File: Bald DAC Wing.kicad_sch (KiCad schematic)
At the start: 54 parts, among them J1 XTRA, J2 DAC_A_Out, J3 DAC_B_Out, J4 Data Debug HDR, J5 Z_Out, SW1 RESET, SW2 XTRA, U1 AD5447, U2 AD8065ARTZ, U3 AD8065ARTZ, U4 74LVC574APWR, U5 74LVC574APWR, U6 74LVC1G04, U7 REF3425

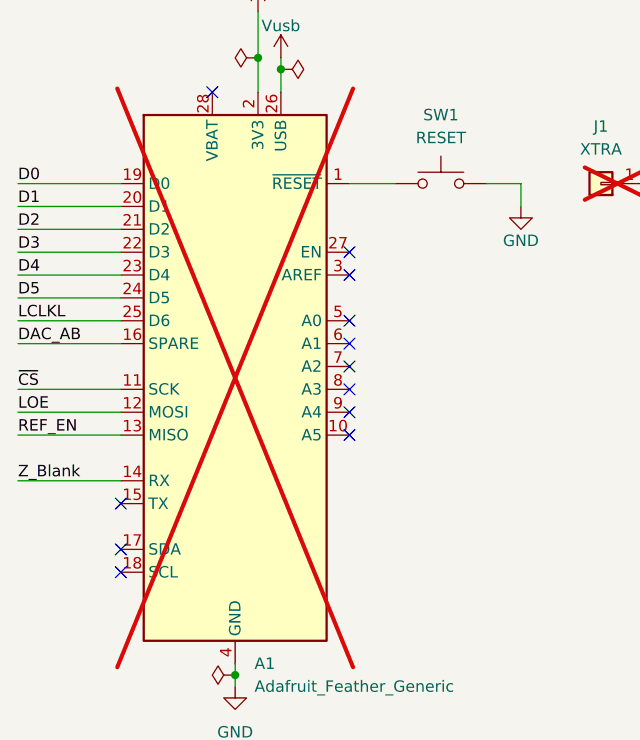
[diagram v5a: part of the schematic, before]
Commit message: only use 1/2 the feather!
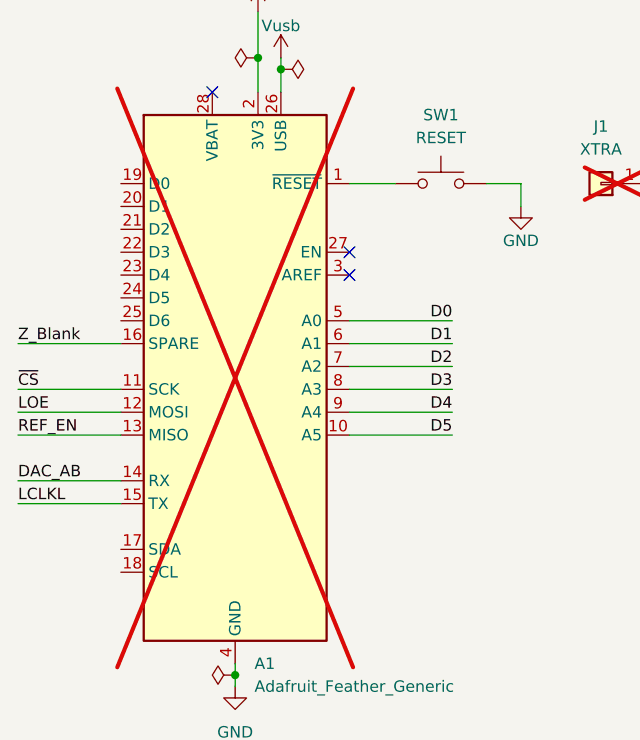
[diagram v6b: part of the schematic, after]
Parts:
- J4: footprint (none) -> Connector_PinHeader_2.00mm:PinHeader_2x16_P2.00mm_Vertical
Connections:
- net D0: now also A1.5 (A0); no longer A1.19 (D0)
- net D1: now also A1.6 (A1); no longer A1.20 (D1)
- net D2: now also A1.7 (A2); no longer A1.21 (D2)
- net D3: now also A1.8 (A3); no longer A1.22 (D3)
- net D4: now also A1.9 (A4); no longer A1.23 (D4)
- net D5: now also A1.10 (A5); no longer A1.24 (D5)
- net DAC_AB: now also A1.14 (RX); no longer A1.16 (SPARE)
- net LCLKL: now also A1.15 (TX); no longer A1.25 (D6)
- net Z_Blank: now also A1.16 (SPARE); no longer A1.14 (RX)
- no-connect marks 12 -> 3
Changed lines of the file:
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@@
 	)
 	(no_connect
-		(at 73.66 182.88)
-	)
-	(no_connect
-		(at 99.06 157.48)
-	)
-	(no_connect
-		(at 73.66 180.34)
-	)
-	(no_connect
-		(at 99.06 154.94)
-	)
-	(no_connect
-		(at 99.06 165.1)
-	)
-	(no_connect
 		(at 83.82 129.54)
 	)
@@
 	)
 	(no_connect
-		(at 73.66 175.26)
-	)
-	(no_connect
-		(at 99.06 167.64)
-	)
-	(no_connect
-		(at 99.06 160.02)
-	)
-	(no_connect
-		(at 99.06 162.56)
-	)
-	(no_connect
 		(at 99.06 147.32)
 	)
@@
 	(wire
 		(pts
-			(xy 62.23 139.7) (xy 73.66 139.7)
+			(xy 110.49 154.94) (xy 99.06 154.94)
 		)
 		(stroke
@@
 	(wire
 		(pts
-			(xy 62.23 154.94) (xy 73.66 154.94)
+			(xy 62.23 175.26) (xy 73.66 175.26)
 		)
 		(stroke
@@
 	(wire
 		(pts
-			(xy 62.23 147.32) (xy 73.66 147.32)
+			(xy 110.49 162.56) (xy 99.06 162.56)
 		)
 		(stroke
@@
 	(wire
 		(pts
-			(xy 62.23 172.72) (xy 73.66 172.72)
+			(xy 62.23 157.48) (xy 73.66 157.48)
 		)
 		(stroke
@@
 	(wire
 		(pts
-			(xy 62.23 144.78) (xy 73.66 144.78)
+			(xy 110.49 160.02) (xy 99.06 160.02)
 		)
 		(stroke
@@
 	(wire
 		(pts
-			(xy 269.24 87.63) (xy 279.4 87.63)
+			(xy 99.06 167.64) (xy 110.49 167.64)
 		)
 		(stroke
@@
 	(wire
 		(pts
-			(xy 62.23 152.4) (xy 73.66 152.4)
+			(xy 269.24 87.63) (xy 279.4 87.63)
 		)
 		(stroke
@@
 	(wire
 		(pts
-			(xy 62.23 142.24) (xy 73.66 142.24)
+			(xy 110.49 157.48) (xy 99.06 157.48)
 		)
 		(stroke
@@
 	(wire
 		(pts
-			(xy 62.23 149.86) (xy 73.66 149.86)
+			(xy 110.49 165.1) (xy 99.06 165.1)
 		)
 		(stroke
@@
 	(wire
 		(pts
-			(xy 62.23 157.48) (xy 73.66 157.48)
+			(xy 62.23 172.72) (xy 73.66 172.72)
 		)
 		(stroke
@@
 	)
 	(label "D3"
-		(at 62.23 147.32 0)
+		(at 110.49 162.56 180)
 		(effects
 			(font
 				(size 1.27 1.27)
 			)
-			(justify left bottom)
+			(justify right bottom)
 		)
 	)
@@
 	)
 	(label "D5"
-		(at 62.23 152.4 0)
+		(at 110.49 167.64 180)
 		(effects
 			(font
 				(size 1.27 1.27)
 			)
-			(justify left bottom)
+			(justify right bottom)
 		)
 	)
@@
 	)
 	(label "D0"
-		(at 62.23 139.7 0)
+		(at 110.49 154.94 180)
 		(effects
 			(font
 				(size 1.27 1.27)
 			)
-			(justify left bottom)
+			(justify right bottom)
 		)
 	)
@@
 	)
 	(label "D4"
-		(at 62.23 149.86 0)
+		(at 110.49 165.1 180)
 		(effects
 			(font
 				(size 1.27 1.27)
 			)
-			(justify left bottom)
+			(justify right bottom)
 		)
 	)
@@
 	)
 	(label "D1"
-		(at 62.23 142.24 0)
+		(at 110.49 157.48 180)
 		(effects
 			(font
 				(size 1.27 1.27)
 			)
-			(justify left bottom)
+			(justify right bottom)
 		)
 	)
@@
 	)
 	(label "Z_Blank"
-		(at 62.23 172.72 0)
+		(at 62.23 157.48 0)
 		(effects
 			(font
@@
 	)
 	(label "D2"
-		(at 62.23 144.78 0)
+		(at 110.49 160.02 180)
 		(effects
 			(font
 				(size 1.27 1.27)
 			)
-			(justify left bottom)
+			(justify right bottom)
 		)
 	)
@@
 	)
 	(label "LCLKL"
-		(at 62.23 154.94 0)
+		(at 62.23 175.26 0)
 		(effects
 			(font
@@
 	)
 	(label "DAC_AB"
-		(at 62.23 157.48 0)
+		(at 62.23 172.72 0)
 		(effects
 			(font
@@
 			)
 		)
-		(property "Footprint" ""
+		(property "Footprint" "Connector_PinHeader_2.00mm:PinHeader_2x16_P2.00mm_Vertical"
 			(at 245.11 124.46 0)
 			(hide yes)

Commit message: got rid of the switches
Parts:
- removed J1: XTRA, Connector_PinSocket_2.54mm:PinSocket_1x01_P2.54mm_Vertical, symbol Connector_Generic:Conn_01x01
- removed SW1: RESET, symbol Switch:SW_Push
- removed SW2: XTRA, symbol Switch:SW_Push
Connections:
- net D0: now also U4.9 (D7), U5.7 (D5); no longer U4.2 (D0), U5.2 (D0)
- net D1: now also U4.8 (D6), U5.6 (D4); no longer U4.3 (D1), U5.3 (D1)
- net D2: now also U4.7 (D5), U5.5 (D3); no longer U4.4 (D2), U5.4 (D2)
- net D3: now also U4.6 (D4), U5.4 (D2); no longer U4.5 (D3), U5.5 (D3)
- net D4: now also U4.5 (D3), U5.3 (D1); no longer U4.6 (D4), U5.6 (D4)
- net D5: now also U4.4 (D2), U5.2 (D0); no longer U4.7 (D5), U5.7 (D5)
- net DB10: now also U4.16 (Q3); no longer U4.18 (Q1)
- net DB11: now also U4.17 (Q2); no longer U4.19 (Q0)
- net DB6: now also U4.12 (Q7); no longer U4.14 (Q5)
- net DB7: now also U4.13 (Q6); no longer U4.15 (Q4)
- net DB8: now also U4.14 (Q5); no longer U4.16 (Q3)
- net DB9: now also U4.15 (Q4); no longer U4.17 (Q2)
- net at TP2.1: now also U4.18 (Q1); no longer U4.12 (Q7)
- net at TP1.1: now also U4.19 (Q0); no longer U4.13 (Q6)
- net at R70.2: now also U4.2 (D0); no longer U4.8 (D6)
- net at R69.2: now also U4.3 (D1); no longer U4.9 (D7)
- no-connect marks 3 -> 4
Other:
- moved on the sheet: R69, R70, TP1, TP2

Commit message: added power header
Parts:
- removed D2: PwrB+, LED_SMD:LED_0805_2012Metric_Pad1.15x1.40mm_HandSolder, symbol Device:LED
- removed D3: Vusb, LED_SMD:LED_0805_2012Metric_Pad1.15x1.40mm_HandSolder, symbol Device:LED
- removed R62, R63: 1k, Resistor_SMD:R_0603_1608Metric_Pad0.98x0.95mm_HandSolder, symbol Device:R
- added J1: PWR, Connector_PinHeader_2.54mm:PinHeader_1x02_P2.54mm_Vertical, symbol Connector_Generic:Conn_01x02
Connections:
- net +3V3: now also J1.2 (Pin_2); no longer A1.2 (3V3)
- net GND: now also J4.31 (Pin_31)
- net Vusb: no longer names the net of A1.26 (USB)
- new net: A1.2 (3V3), J1.1 (Pin_1)
- no-connect marks 4 -> 14
